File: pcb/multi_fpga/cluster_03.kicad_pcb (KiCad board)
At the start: 2 copper layers, 161.3 x 208.8 mm, 52 parts, among them U73 Comment, U74 Comment, U75 Comment, U76 Comment, U77 Comment, U78 Comment, U79 Comment, U80 Comment, U81 Comment, U82 Comment, U83 Comment, U84 Comment, U85 Comment, U86 Comment, U87 Comment, U88 Comment, U89 Comment, U90 Comment, U91 Comment, U92 Comment, U93 Comment, U94 Comment, U95 Comment, U96 Comment

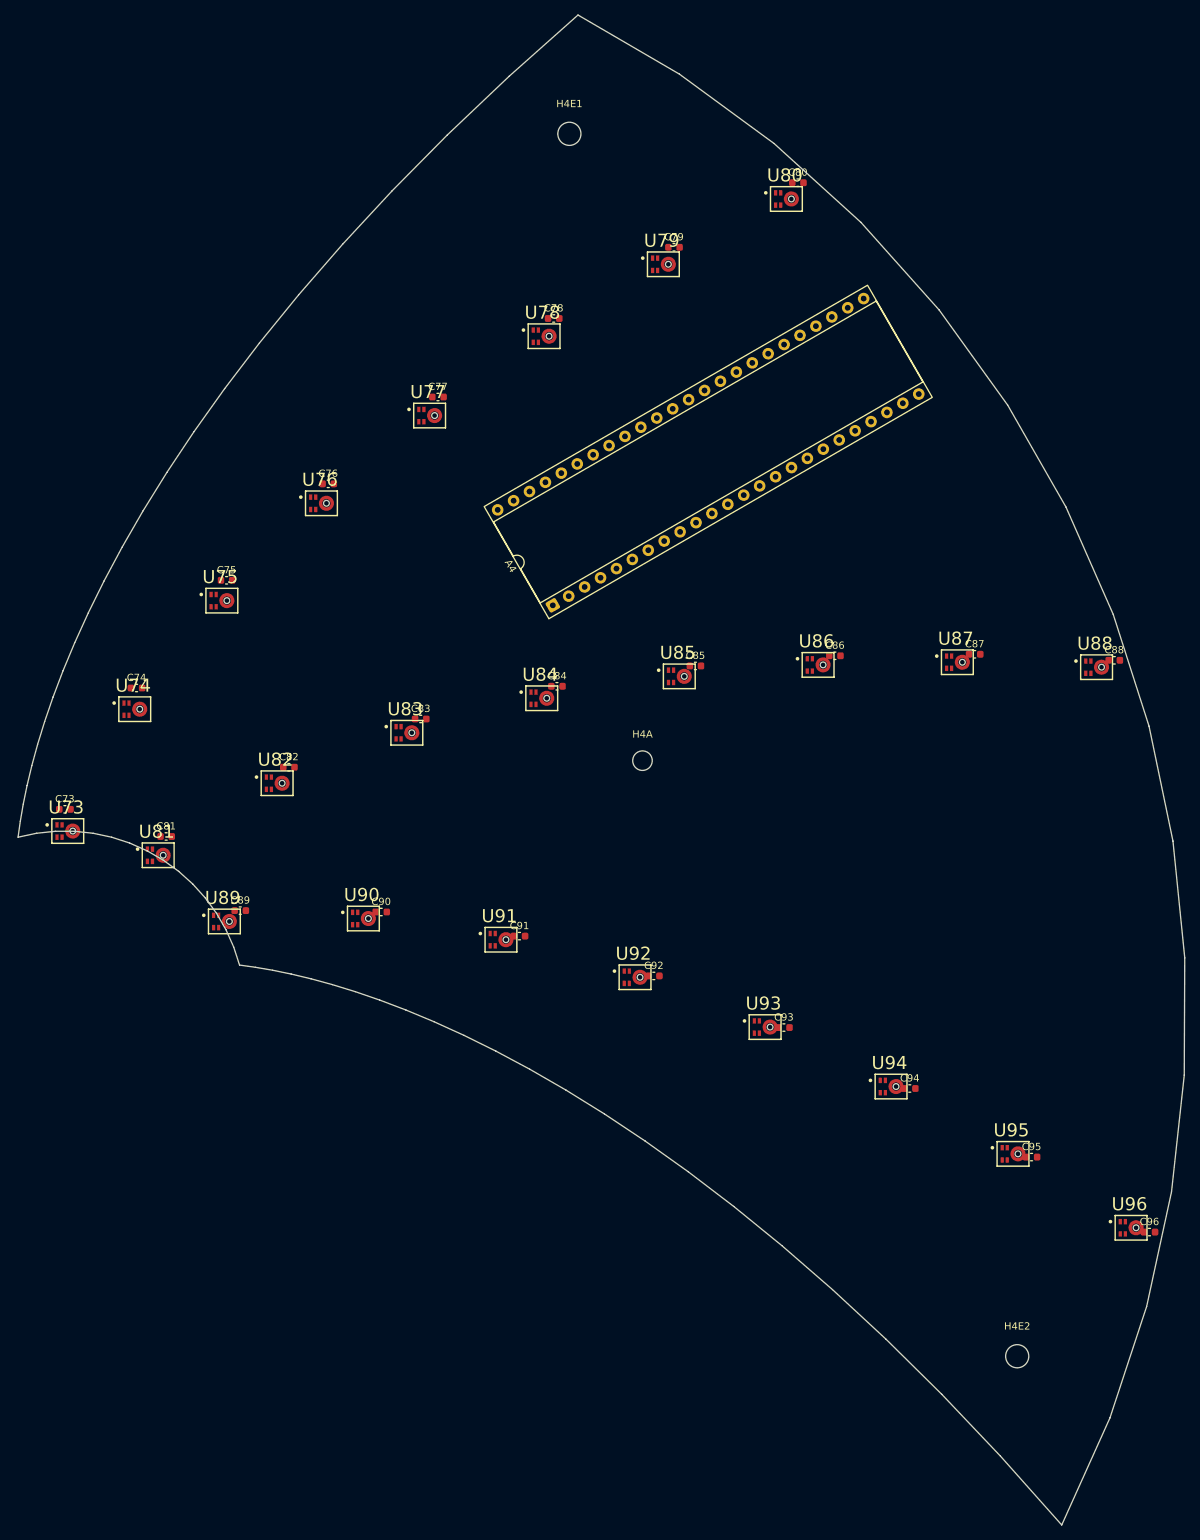
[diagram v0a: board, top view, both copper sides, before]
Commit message: Fixed inner circle of mics.
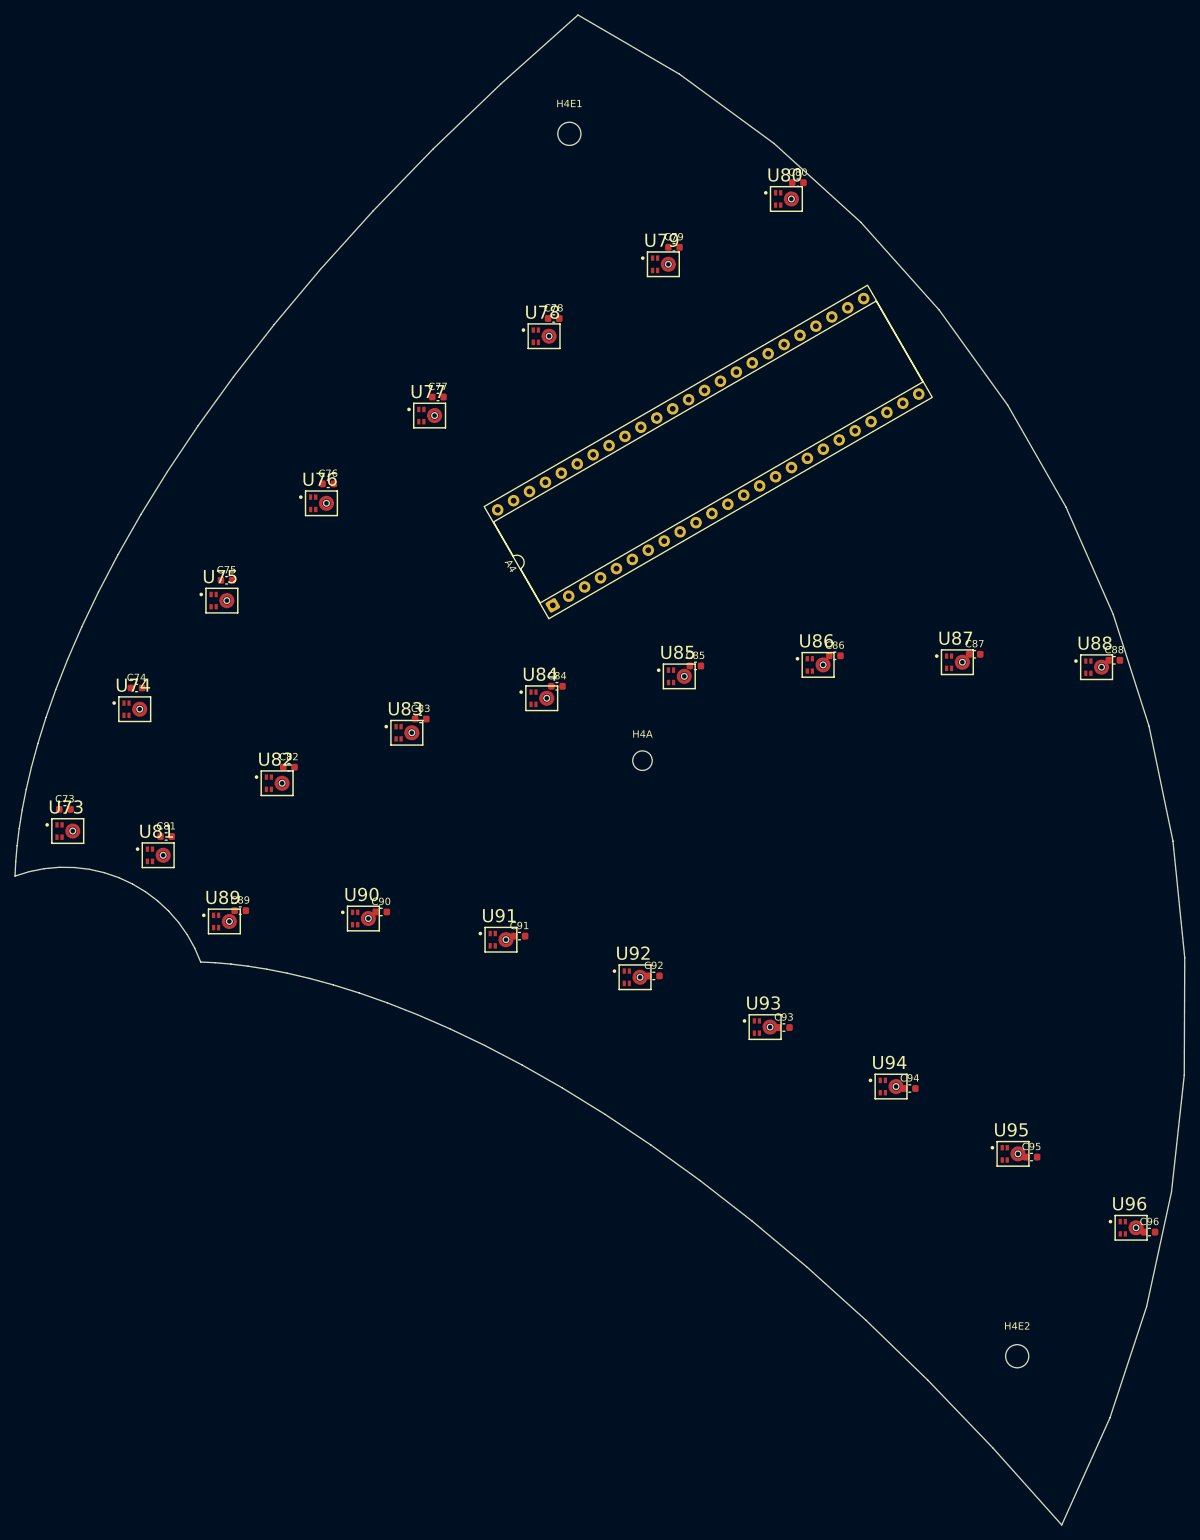
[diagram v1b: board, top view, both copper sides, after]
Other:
- board size 161.3 x 208.8 mm -> 161.7 x 208.8 mm
